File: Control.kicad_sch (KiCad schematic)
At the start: 18 parts, among them J4 DBG, U1 XC95144XL-TQ100, U29 74LVC1G34GW

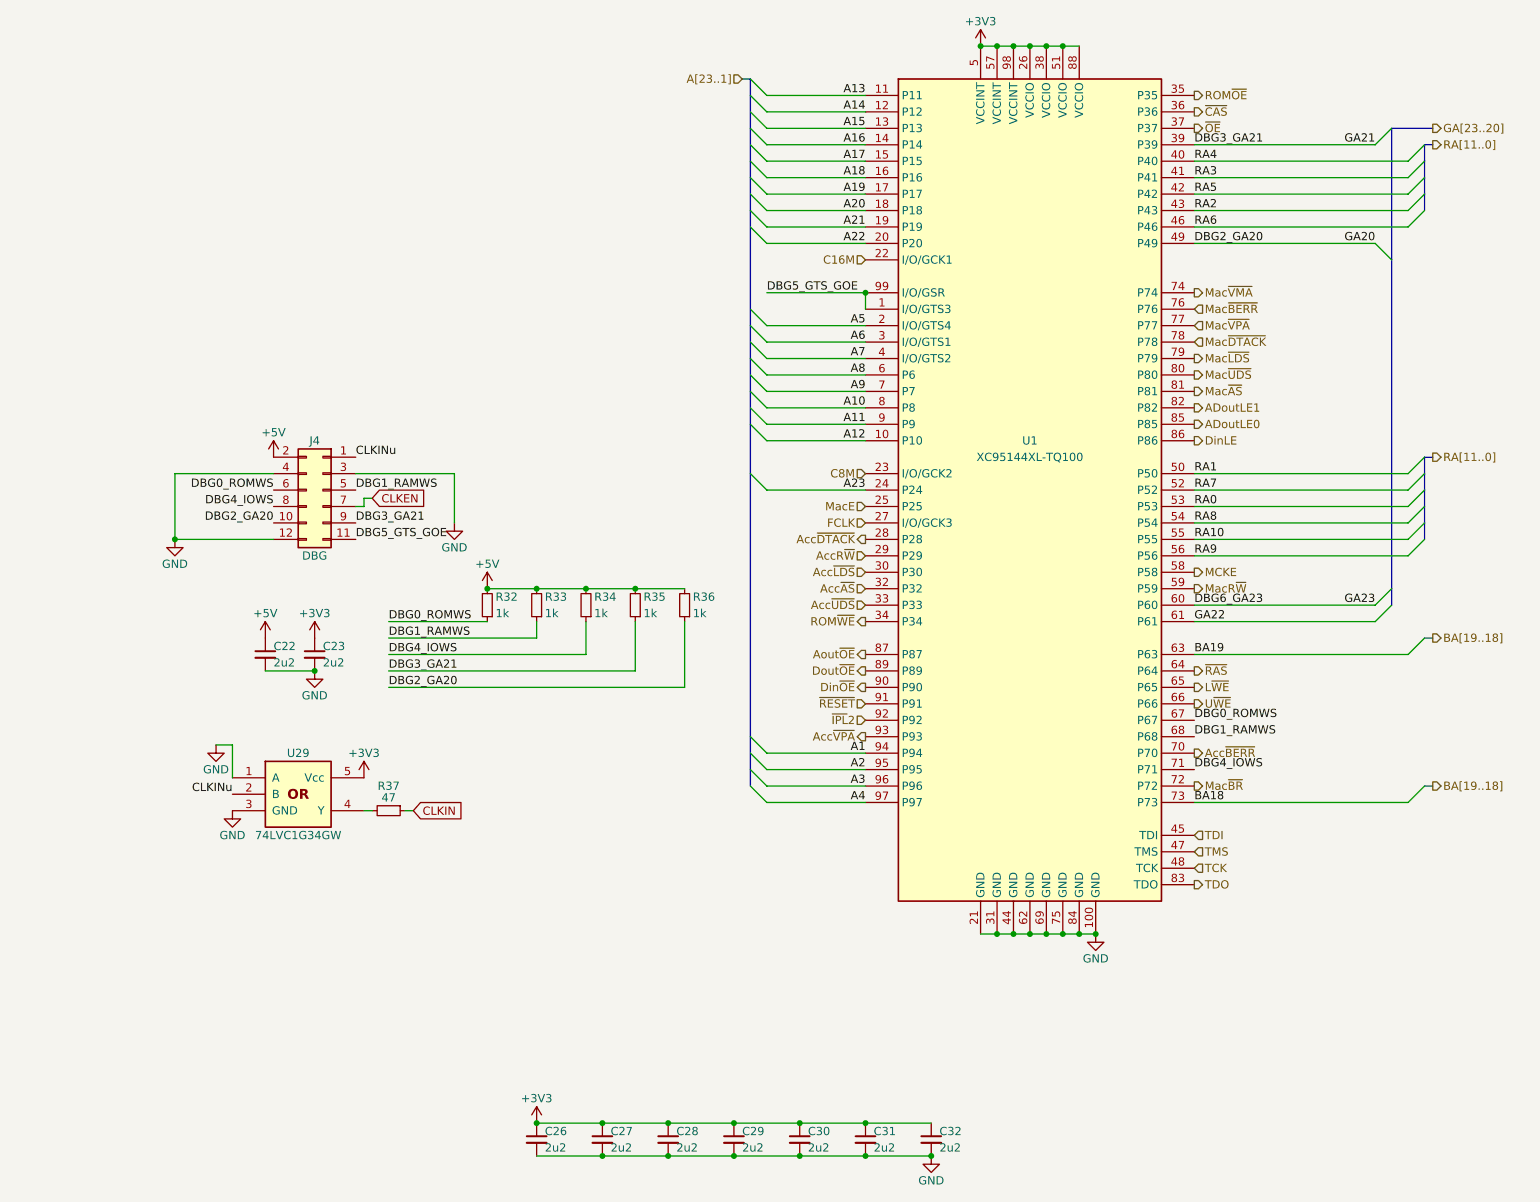
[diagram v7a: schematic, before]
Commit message: Before remove first clock input buffer
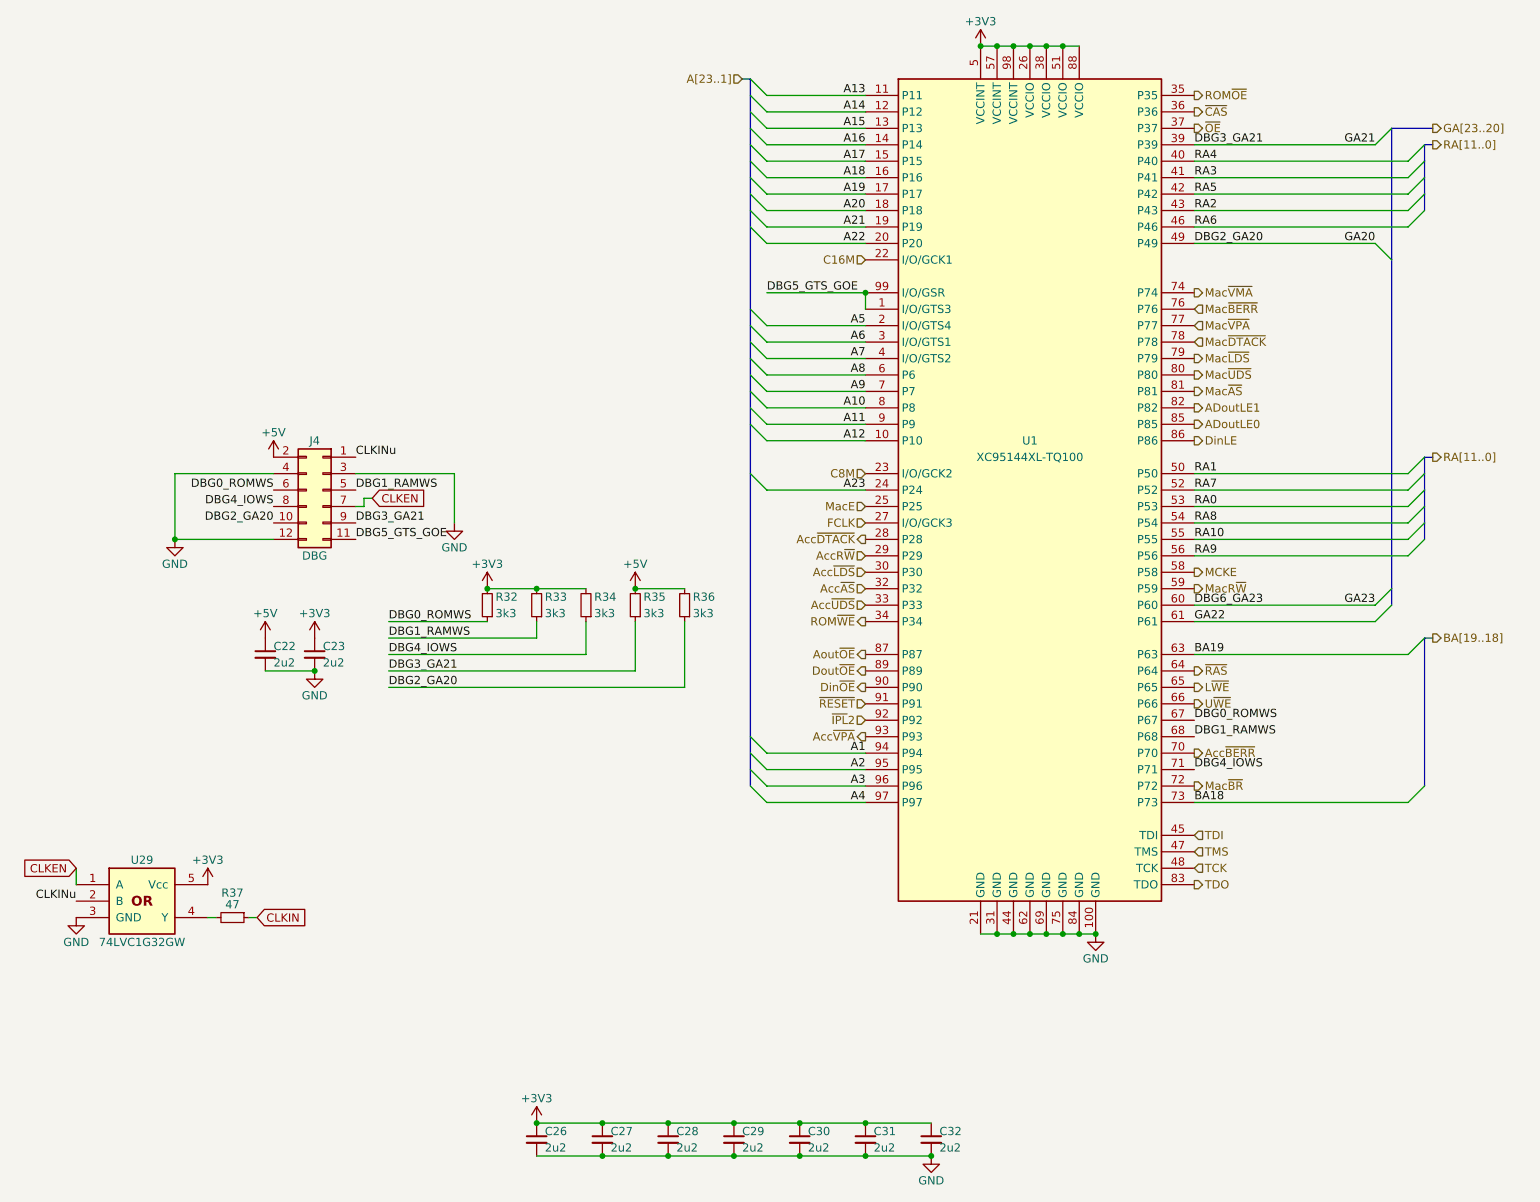
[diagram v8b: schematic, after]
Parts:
- R32, R33, R34, R35, R36: value 1k -> 3k3
- U29: value 74LVC1G34GW -> 74LVC1G32GW; LCSC Part C455045 -> C12516
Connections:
- net +3V3: now also R32.2, R33.2, R34.2
- net +5V: no longer R32.2, R33.2, R34.2
- net CLKEN: now also U29.1 (A)
- net GND: no longer U29.1 (A)
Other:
- moved on the sheet: R37
